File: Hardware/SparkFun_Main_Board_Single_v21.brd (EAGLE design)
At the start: 86.4 x 73.7 mm, 130 parts, among them J1 MICROMOD-2222-C, J10 MICRO-SD-PUSH-PUSH-EXT-PIN, J2 Vertical Qwiic Connector, J4 QWIIC_RIGHT_ANGLE, J5 CORTEX_JTAG_DEBUG_MINIMUM_PTH, J6 MICROMOD_FUNCTION_MAIN, Q1 3.1A/30V/105mΩ, Q2 20V/4.2A/52mΩ/1.4W, U1 STG3856QTR, U2 MCP73831, U3 ESD Diode, U4 AP7347DQ-33W5-7K-3.3V, U5 AP7361C-33

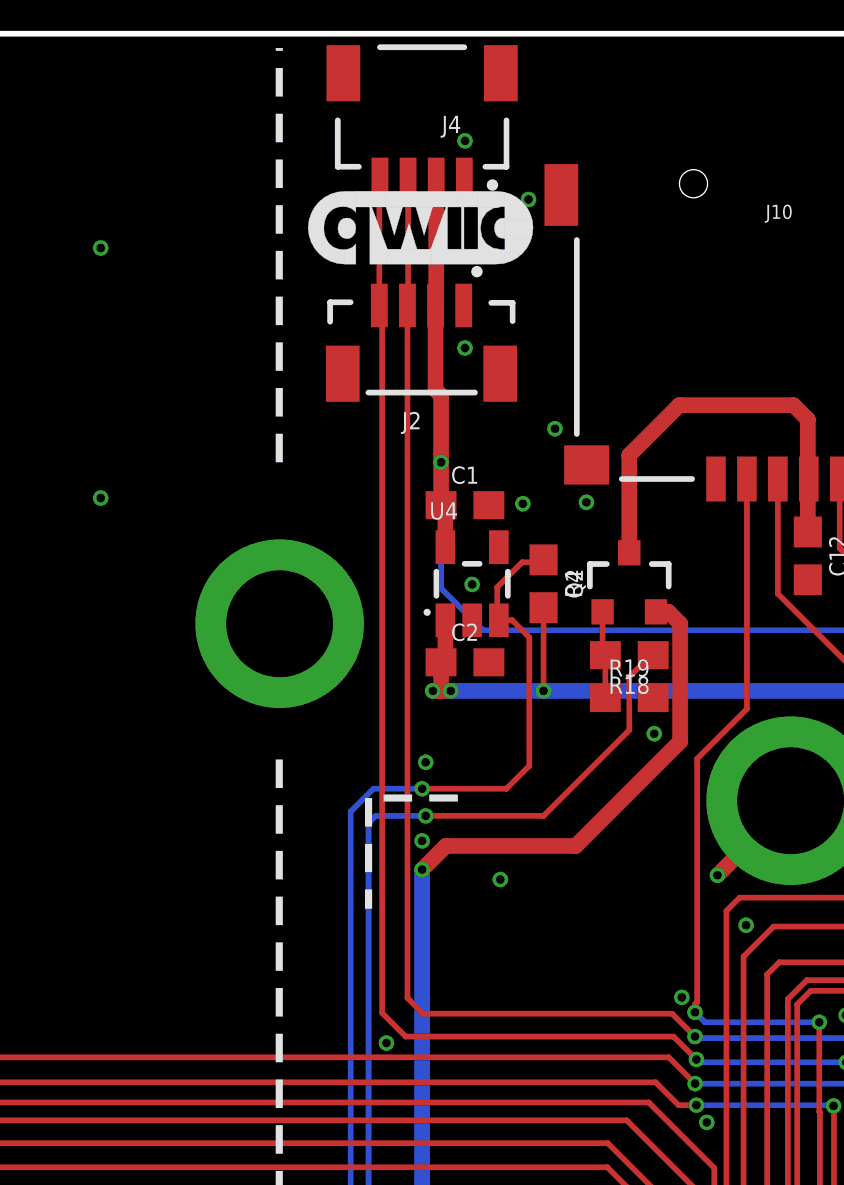
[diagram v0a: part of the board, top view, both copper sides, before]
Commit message: Updates function board symbol
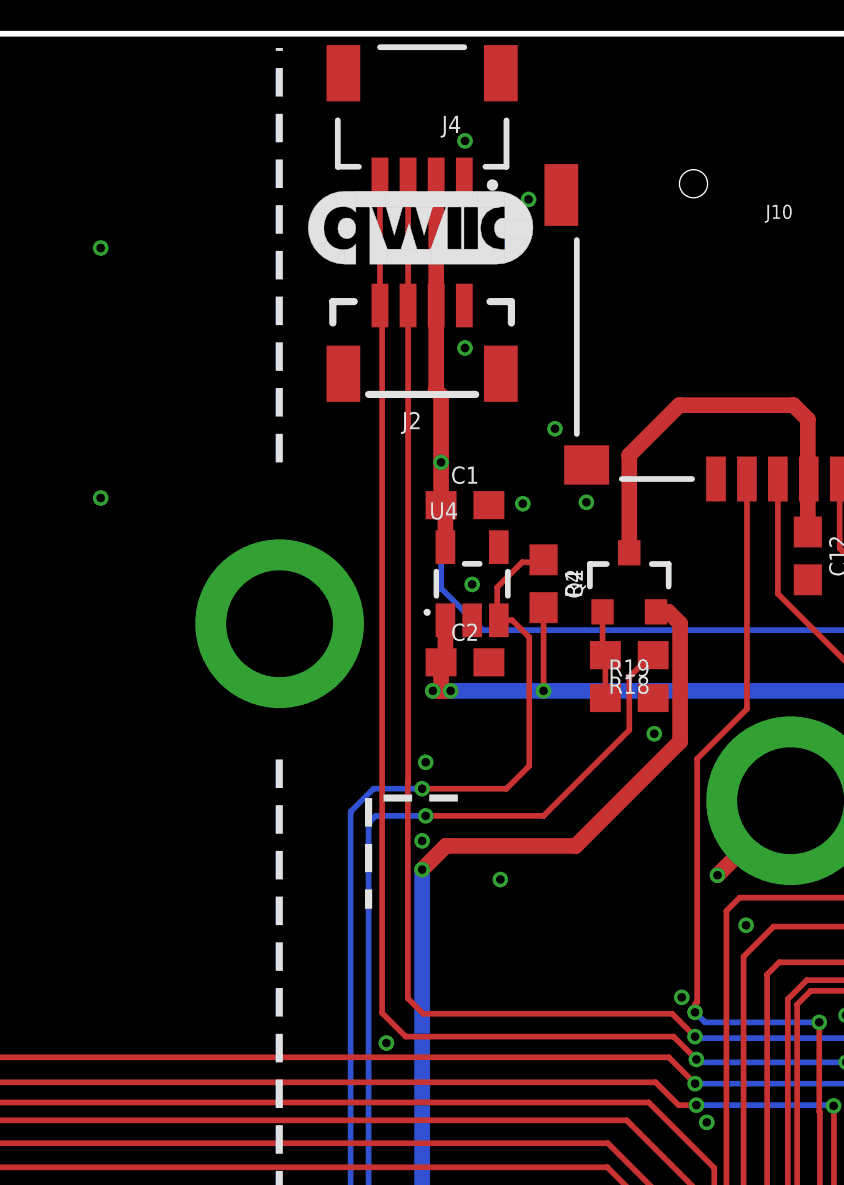
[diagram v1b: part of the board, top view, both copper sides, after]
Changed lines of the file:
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@@
 <contactref element="J6" pad="21"/>
 <contactref element="R15" pad="1"/>
-<wire x1="46.738" y1="63.995" x2="46.738" y2="68.558" width="0.2032" layer="1"/>
 <wire x1="29.1338" y1="7.1628" x2="38.227" y2="7.1628" width="0.2032" layer="16"/>
-<wire x1="46.738" y1="63.995" x2="46.8376" y2="63.8954" width="0.2032" layer="1"/>
-<wire x1="46.8376" y1="63.8954" x2="46.8376" y2="38.8366" width="0.2032" layer="1"/>
 <wire x1="60.4266" y1="24.5364" x2="60.4266" y2="10.886825" width="0.2032" layer="1"/>
 <via x="38.227" y="7.1628" extent="1-16" drill="0.3048"/>
@@
 <wire x1="62.992" y1="10.502" x2="60.811425" y2="10.502" width="0.2032" layer="1"/>
 <wire x1="60.811425" y1="10.502" x2="60.4266" y2="10.886825" width="0.2032" layer="1"/>
+<wire x1="46.76" y1="63.995" x2="46.76" y2="68.58" width="0.2032" layer="1"/>
+<wire x1="46.76" y1="63.995" x2="46.8376" y2="63.9174" width="0.2032" layer="1"/>
+<wire x1="46.8376" y1="63.9174" x2="46.8376" y2="38.8366" width="0.2032" layer="1"/>
 </signal>
 <signal name="I2C_SDA">
@@
 <wire x1="57.15" y1="38.8112" x2="57.9628" y2="37.9984" width="0.2032" layer="1"/>
 <wire x1="48.2968" y1="38.8112" x2="57.15" y2="38.8112" width="0.2032" layer="1"/>
-<wire x1="47.76" y1="64.017" x2="47.738" y2="63.995" width="0.2032" layer="1"/>
 <contactref element="J6" pad="19"/>
 <contactref element="R14" pad="1"/>
-<wire x1="47.76" y1="68.58" x2="47.76" y2="64.017" width="0.2032" layer="1"/>
+<wire x1="47.76" y1="68.58" x2="47.76" y2="63.995" width="0.2032" layer="1"/>
 <wire x1="28.88" y1="6.274" x2="28.88" y2="5.139" width="0.2032" layer="1"/>
 <wire x1="39.0271" y1="6.4389" x2="62.3189" y2="6.4389" width="0.2032" layer="1"/>
@@
 <wire x1="58.016" y1="37.9452" x2="57.9628" y2="37.9984" width="0.2032" layer="16"/>
 <via x="57.9628" y="37.9984" extent="1-16" drill="0.3048"/>
-<wire x1="47.738" y1="63.995" x2="47.738" y2="39.37" width="0.2032" layer="1"/>
-<wire x1="47.738" y1="39.37" x2="48.2968" y2="38.8112" width="0.2032" layer="1"/>
+<wire x1="47.752" y1="39.356" x2="48.2968" y2="38.8112" width="0.2032" layer="1"/>
 <wire x1="62.3189" y1="6.4389" x2="64.1016" y2="8.2216" width="0.2032" layer="1"/>
 <wire x1="64.1016" y1="8.2216" x2="64.1016" y2="9.3646" width="0.2032" layer="1"/>
@@
 <wire x1="65.0796" y1="9.5806" x2="65.278" y2="9.779" width="0.2032" layer="1"/>
 <wire x1="65.278" y1="9.779" x2="65.278" y2="10.502" width="0.2032" layer="1"/>
+<wire x1="47.76" y1="63.995" x2="47.76" y2="47.030625" width="0.2032" layer="1"/>
+<wire x1="47.76" y1="47.030625" x2="47.752" y2="47.022625" width="0.2032" layer="1"/>
+<wire x1="47.752" y1="47.022625" x2="47.752" y2="39.356" width="0.2032" layer="1"/>
 </signal>
 <signal name="HOST_D-" class="2">
@@
 <wire x1="48.934" y1="56.896" x2="48.934" y2="58.42" width="0.5588" layer="1"/>
 <wire x1="48.934" y1="58.42" x2="48.934" y2="60.794" width="0.5588" layer="1"/>
-<wire x1="48.738" y1="60.99" x2="48.738" y2="63.995" width="0.5588" layer="1"/>
-<wire x1="48.934" y1="60.794" x2="48.738" y2="60.99" width="0.5588" layer="1"/>
-<wire x1="48.76" y1="68.58" x2="48.76" y2="64.017" width="0.5588" layer="1"/>
-<wire x1="48.76" y1="64.017" x2="48.738" y2="63.995" width="0.5588" layer="1"/>
+<wire x1="48.738" y1="60.99" x2="48.934" y2="60.794" width="0.5588" layer="1"/>
+<wire x1="48.76" y1="68.58" x2="48.76" y2="63.995" width="0.5588" layer="1"/>
 <contactref element="R17" pad="2"/>
 <via x="81.153" y="52.451" extent="1-16" drill="0.3048"/>
@@
 <wire x1="48.934" y1="56.896" x2="49.088" y2="56.742" width="0.5588" layer="1"/>
 <wire x1="49.088" y1="56.742" x2="49.088" y2="55.4021" width="0.5588" layer="1"/>
+<wire x1="48.76" y1="63.995" x2="48.76" y2="61.012" width="0.5588" layer="1"/>
+<wire x1="48.76" y1="61.012" x2="48.738" y2="60.99" width="0.5588" layer="1"/>
 </signal>
 <signal name="PWR_EN0">
